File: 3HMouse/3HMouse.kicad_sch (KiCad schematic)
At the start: 85 parts, among them J1 USB_C_Receptacle_USB2.0, SW1 CherryMX, SW10 CherryMX, SW11 CherryMX, SW12 CherryMX, SW13 CherryMX, SW14 CherryMX, SW15 CherryMX, SW16 CherryMX, SW17 CherryMX, SW18 CherryMX, SW19 CherryMX, SW2 CherryMX, SW20 CherryMX, SW21 CherryMX, SW22 CherryMX, SW23 CherryMX, SW24 CherryMX, SW25 CherryMX, SW26 CherryMX, SW27 CherryMX, SW28 CherryMX, SW29 CherryMX, SW3 CherryMX, SW30 RotaryEncoder, SW31 RotaryEncoder, SW32 Reset, SW4 CherryMX, SW5 CherryMX, SW6 CherryMX, SW7 CherryMX, SW8 CherryMX, SW9 CherryMX, U1 AT90USB1286-A, U2 USBLC6-2SC6, Y1 16 MHz

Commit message: v0.4.0 final
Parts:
- removed SW32: Reset, random-keyboard-parts:SKQG-1155865, symbol Switch:SW_Push
- removed U1: AT90USB1286-A, Package_QFP:TQFP-64_14x14mm_P0.8mm, symbol MCU_Microchip_AVR:AT90USB1286-A
- added S2: TS-1187A-B-A-B, SW_TS-1187A-B-A-B:SW_TS-1187A-B-A-B, symbol TS-1187A-B-A-B:TS-1187A-B-A-B
- added U1: ATmega32U4-M, Package_DFN_QFN:QFN-44-1EP_7x7mm_P0.5mm_EP5.2x5.2mm, symbol MCU_Microchip_ATmega:ATmega32U4-M
- J1: footprint Connector_USB:USB_C_Receptacle_GCT_USB4085 -> USB_C_Receptacle_GT-USB-7010:USB_C_Receptacle_GT-USB-7010
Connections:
- net +5V: now also C3.1, U1.14 (VCC), U1.2 (UVCC), U1.24 (AVCC), U1.34 (VCC), U1.44 (AVCC), U1.7 (VBUS); no longer C3.2
- net COL0: now also U1.11 (PB3)
- net COL1: now also U1.19 (PD1)
- net COL10: now also U1.1 (PE6)
- net COL2: now also U1.20 (PD2)
- net COL3: now also U1.21 (PD3)
- net COL4: now also U1.22 (PD5)
- net COL5: now also U1.36 (PF7)
- net COL6: now also U1.25 (PD4)
- net COL7: now also U1.26 (PD6)
- net COL8: now also U1.27 (PD7)
- net COL9: now also U1.28 (PB4)
- net GND: now also C3.2, C4.1, C5.1, C6.1, R5.2, S2.A, S2.B, U1.15 (GND), U1.23 (GND), U1.35 (GND), U1.43 (GND), U1.45 (GND), U1.5 (UGND); no longer R5.1
- net HOR: now also U1.40 (PF1)
- net RE0A: now also U1.30 (PB6)
- net RE0B: now also U1.29 (PB5)
- net RE1A: now also U1.32 (PC7)
- net RE1B: now also U1.31 (PC6)
- net ROW0: now also U1.9 (PB1)
- net ROW1: now also U1.10 (PB2)
- net ROW2: now also U1.12 (PB7)
- net ROW3: now also U1.8 (PB0)
- net ROW4: now also U1.39 (PF4)
- net SCL: now also U1.37 (PF6)
- net SDA: now also U1.38 (PF5)
- net VER: now also U1.41 (PF0)
- net XTAL1: now reaches C1.1, Y1.1
- net XTAL1: now also U1.17 (XTAL1)
- net D-F: now reaches R2.2
- net D-F: now also U1.3 (D-)
- net XTAL2: now reaches C2.1, Y1.3
- net XTAL2: now also U1.16 (XTAL2)
- net RESET: now reaches R6.2
- net RESET: now also S2.C, S2.D, U1.13 (~{RESET})
- net D+F: now reaches R1.2
- net D+F: now also U1.4 (D+)
- net UCAP: now reaches C8.2
- net UCAP: now also U1.6 (UCAP)
- new net: R5.1, U1.33 (~{HWB}/PE2)
- no-connect marks 34 -> 12
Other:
- moved on the sheet: C3, C4, C5, C6, C7, C8, R5, R6

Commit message: Placements done for v2
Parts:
- removed D20, D21, D22, D23, D24, D25, D26, D27, D28, D29, D35: D_Small, Diode_SMD:D_SOD-123, symbol Device:D_Small
- removed SW20, SW21, SW22, SW23, SW24, SW25, SW26, SW27, SW28, SW29: CherryMX, MX_Only:MXOnly-1U-NoLED, symbol CherryMX:CherryMX
- removed SW30, SW31: RotaryEncoder, Keebio-Parts:RotaryEncoder_EC11, symbol Device:RotaryEncoder
- added D0_3, D1_3, D2_3, D5_0, D5_1, D5_2, D5_3, D5_4, D6_0, D6_1, D6_2, D6_3, D6_4: D_Small, Diode_SMD:D_SOD-123, symbol Device:D_Small
- added DL0_0, DL0_1, DL0_2, DL1_0, DL1_1, DL1_2, DL2_0, DL2_1, DL2_2, DL3_0, DL3_1, DL3_2, DL3_3, DL3_4, DL4_0, DL4_1, DL4_2, DL4_3, DL4_4, DL5_0, DL5_1, DL5_2, DL5_3, DL5_4, DL6_0, DL6_1, DL6_2, DL6_3, DL6_4: SK6805-EC15, HLibrary:SK6805-EC15, symbol HLibrary:SK6805-EC15
- added R8: 500, Resistor_SMD:R_0805_2012Metric, symbol Device:R_Small
- added RE1, RE2: RotaryEncoder_Switch, Rotary_Encoder:RotaryEncoder_Alps_EC11E-Switch_Vertical_H20mm, symbol Device:RotaryEncoder_Switch
- added SW5_0, SW5_1, SW5_2, SW5_3, SW5_4, SW6_0, SW6_1, SW6_2, SW6_3, SW6_4: CherryMX, MX_Only:MXOnly-1U-Hotswap, symbol CherryMX:CherryMX
- SW0_0: renamed from SW1; footprint MX_Only:MXOnly-1U-NoLED -> MX_Only:MXOnly-1U-Hotswap
- SW0_1: renamed from SW6; footprint MX_Only:MXOnly-1U-NoLED -> MX_Only:MXOnly-1U-Hotswap
- SW0_2: renamed from SW11; footprint MX_Only:MXOnly-1U-NoLED -> MX_Only:MXOnly-1U-Hotswap
- SW1_0: renamed from SW2; footprint MX_Only:MXOnly-1U-NoLED -> MX_Only:MXOnly-1U-Hotswap
- SW1_1: renamed from SW7; footprint MX_Only:MXOnly-1U-NoLED -> MX_Only:MXOnly-1U-Hotswap
- SW1_2: renamed from SW12; footprint MX_Only:MXOnly-1U-NoLED -> MX_Only:MXOnly-1U-Hotswap
- SW2_0: renamed from SW3; footprint MX_Only:MXOnly-1U-NoLED -> MX_Only:MXOnly-1U-Hotswap
- SW2_1: renamed from SW8; footprint MX_Only:MXOnly-1U-NoLED -> MX_Only:MXOnly-1U-Hotswap
- SW2_2: renamed from SW13; footprint MX_Only:MXOnly-1U-NoLED -> MX_Only:MXOnly-1U-Hotswap
- SW3_0: renamed from SW4; footprint MX_Only:MXOnly-1.5U-NoLED -> MX_Only:MXOnly-1U-Hotswap
- SW3_1: renamed from SW9; footprint MX_Only:MXOnly-1U-NoLED -> MX_Only:MXOnly-1U-Hotswap
- SW3_2: renamed from SW14; footprint MX_Only:MXOnly-1U-NoLED -> MX_Only:MXOnly-1U-Hotswap
- SW3_3: renamed from SW16; footprint MX_Only:MXOnly-1U-NoLED -> MX_Only:MXOnly-1U-Hotswap
- SW3_4: renamed from SW18; footprint MX_Only:MXOnly-1U-NoLED -> MX_Only:MXOnly-1U-Hotswap
- SW4_0: renamed from SW5; footprint MX_Only:MXOnly-1.25U-NoLED -> MX_Only:MXOnly-1U-Hotswap
- SW4_1: renamed from SW10; footprint MX_Only:MXOnly-1.25U-NoLED -> MX_Only:MXOnly-1U-Hotswap
- SW4_2: renamed from SW15; footprint MX_Only:MXOnly-1U-NoLED -> MX_Only:MXOnly-1U-Hotswap
- SW4_3: renamed from SW17; footprint MX_Only:MXOnly-1U-NoLED -> MX_Only:MXOnly-1U-Hotswap
- SW4_4: renamed from SW19; footprint MX_Only:MXOnly-1U-NoLED -> MX_Only:MXOnly-1U-Hotswap
- renumbered D1 to D0_0, D6 to D0_1, D11 to D0_2, D2 to D1_0, D7 to D1_1, D12 to D1_2, D3 to D2_0, D8 to D2_1, D13 to D2_2, D4 to D3_0, D9 to D3_1, D14 to D3_2, D16 to D3_3, D18 to D3_4, D5 to D4_0, D10 to D4_1, D15 to D4_2, D17 to D4_3, D19 to D4_4
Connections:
- net +5V: now also DL0_0.2 (VDD), DL0_1.2 (VDD), DL0_2.2 (VDD), DL1_0.2 (VDD), DL1_1.2 (VDD), DL1_2.2 (VDD), DL2_0.2 (VDD), DL2_1.2 (VDD), DL2_2.2 (VDD), DL3_0.2 (VDD), DL3_1.2 (VDD), DL3_2.2 (VDD), DL3_3.2 (VDD), DL3_4.2 (VDD), DL4_0.2 (VDD), DL4_1.2 (VDD), DL4_2.2 (VDD), DL4_3.2 (VDD), DL4_4.2 (VDD), DL5_0.2 (VDD), DL5_1.2 (VDD), DL5_2.2 (VDD), DL5_3.2 (VDD), DL5_4.2 (VDD), DL6_0.2 (VDD), DL6_1.2 (VDD), DL6_2.2 (VDD), DL6_3.2 (VDD), DL6_4.2 (VDD)
- net COL0: now also SW5_0.2, SW6_0.2
- net COL1: now also SW5_1.2, SW6_1.2
- net COL2: now also SW5_2.2, SW6_2.2
- net COL3: now also S1.C1, RE1.S1, RE2.S1, SW5_3.2, SW6_3.2
- net COL4: now also SW5_4.2, SW6_4.2
- net GND: now also DL0_0.4 (GND), DL0_1.4 (GND), DL0_2.4 (GND), DL1_0.4 (GND), DL1_1.4 (GND), DL1_2.4 (GND), DL2_0.4 (GND), DL2_1.4 (GND), DL2_2.4 (GND), DL3_0.4 (GND), DL3_1.4 (GND), DL3_2.4 (GND), DL3_3.4 (GND), DL3_4.4 (GND), DL4_0.4 (GND), DL4_1.4 (GND), DL4_2.4 (GND), DL4_3.4 (GND), DL4_4.4 (GND), DL5_0.4 (GND), DL5_1.4 (GND), DL5_2.4 (GND), DL5_3.4 (GND), DL5_4.4 (GND), DL6_0.4 (GND), DL6_1.4 (GND), DL6_2.4 (GND), DL6_3.4 (GND), DL6_4.4 (GND), RE1.C, RE2.C
- net RE0A: now also RE1.A
- net RE0B: now also RE1.B
- net RE1A: now also RE2.A
- net RE1B: now also RE2.B
- net ROW0: now also D0_3.1 (K)
- net ROW1: now also D1_3.1 (K)
- net ROW2: now also D2_3.1 (K)
- net LED: now reaches U1.18 (PD0)
- net LED: now also R8.1
- net at S1.D1: now also D0_3.2 (A)
- net COL10: no longer names the net of U1.1 (PE6)
- net COL10: no longer S1.C1
- net COL5: no longer names the net of U1.36 (PF7)
- net COL6 renamed ROW6
- net ROW6: now also D6_0.1 (K), D6_1.1 (K), D6_2.1 (K), D6_3.1 (K), D6_4.1 (K)
- net COL7: no longer names the net of U1.26 (PD6)
- net COL8: no longer names the net of U1.27 (PD7)
- net COL9 renamed ROW5
- net ROW5: now also D5_0.1 (K), D5_1.1 (K), D5_2.1 (K), D5_3.1 (K), D5_4.1 (K)
- new net: D6_2.2 (A), SW6_2.1
- new net: DL2_1.3 (DOUT), DL2_2.1 (DIN)
- new net: DL2_2.3 (DOUT), DL3_0.1 (DIN)
- new net: D6_3.2 (A), SW6_3.1
- new net: DL3_3.3 (DOUT), DL3_4.1 (DIN)
- new net: DL3_4.3 (DOUT), DL4_0.1 (DIN)
- new net: DL1_0.3 (DOUT), DL1_1.1 (DIN)
- new net: DL1_1.3 (DOUT), DL1_2.1 (DIN)
- new net: D5_0.2 (A), SW5_0.1
- new net: D6_4.2 (A), SW6_4.1
- new net: DL4_4.3 (DOUT), DL5_0.1 (DIN)
- new net: DL5_0.3 (DOUT), DL5_1.1 (DIN)
- new net: DL0_2.3 (DOUT), DL1_0.1 (DIN)
- new net: D6_1.2 (A), SW6_1.1
- new net: D2_3.2 (A), RE2.S2
- new net: DL4_0.3 (DOUT), DL4_1.1 (DIN)
- new net: DL4_1.3 (DOUT), DL4_2.1 (DIN)
- new net: DL0_0.1 (DIN), R8.2
- new net: DL0_0.3 (DOUT), DL0_1.1 (DIN)
- new net: DL5_2.3 (DOUT), DL5_3.1 (DIN)
- new net: DL5_3.3 (DOUT), DL5_4.1 (DIN)
- new net: DL3_0.3 (DOUT), DL3_1.1 (DIN)
- new net: DL4_2.3 (DOUT), DL4_3.1 (DIN)
- new net: DL4_3.3 (DOUT), DL4_4.1 (DIN)
- new net: D1_3.2 (A), RE1.S2
- new net: DL1_2.3 (DOUT), DL2_0.1 (DIN)
- new net: DL2_0.3 (DOUT), DL2_1.1 (DIN)
- new net: D6_0.2 (A), SW6_0.1
- new net: DL6_2.3 (DOUT), DL6_3.1 (DIN)
- new net: DL6_3.3 (DOUT), DL6_4.1 (DIN)
- new net: DL3_1.3 (DOUT), DL3_2.1 (DIN)
- new net: D5_2.2 (A), SW5_2.1
- new net: D5_3.2 (A), SW5_3.1
- new net: D5_1.2 (A), SW5_1.1
- new net: DL0_1.3 (DOUT), DL0_2.1 (DIN)
- new net: D5_4.2 (A), SW5_4.1
- new net: DL5_4.3 (DOUT), DL6_0.1 (DIN)
- new net: DL3_2.3 (DOUT), DL3_3.1 (DIN)
- new net: DL6_0.3 (DOUT), DL6_1.1 (DIN)
- new net: DL6_1.3 (DOUT), DL6_2.1 (DIN)
- new net: DL5_1.3 (DOUT), DL5_2.1 (DIN)
- no-connect marks 12 -> 16
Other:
- note added: "RGB LEDs"
- note removed: "3HMouse"
- moved on the sheet: Brd1, C1, C2, C3, C4, C5, C6, C7, C8, D0_0, D0_1, D0_2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

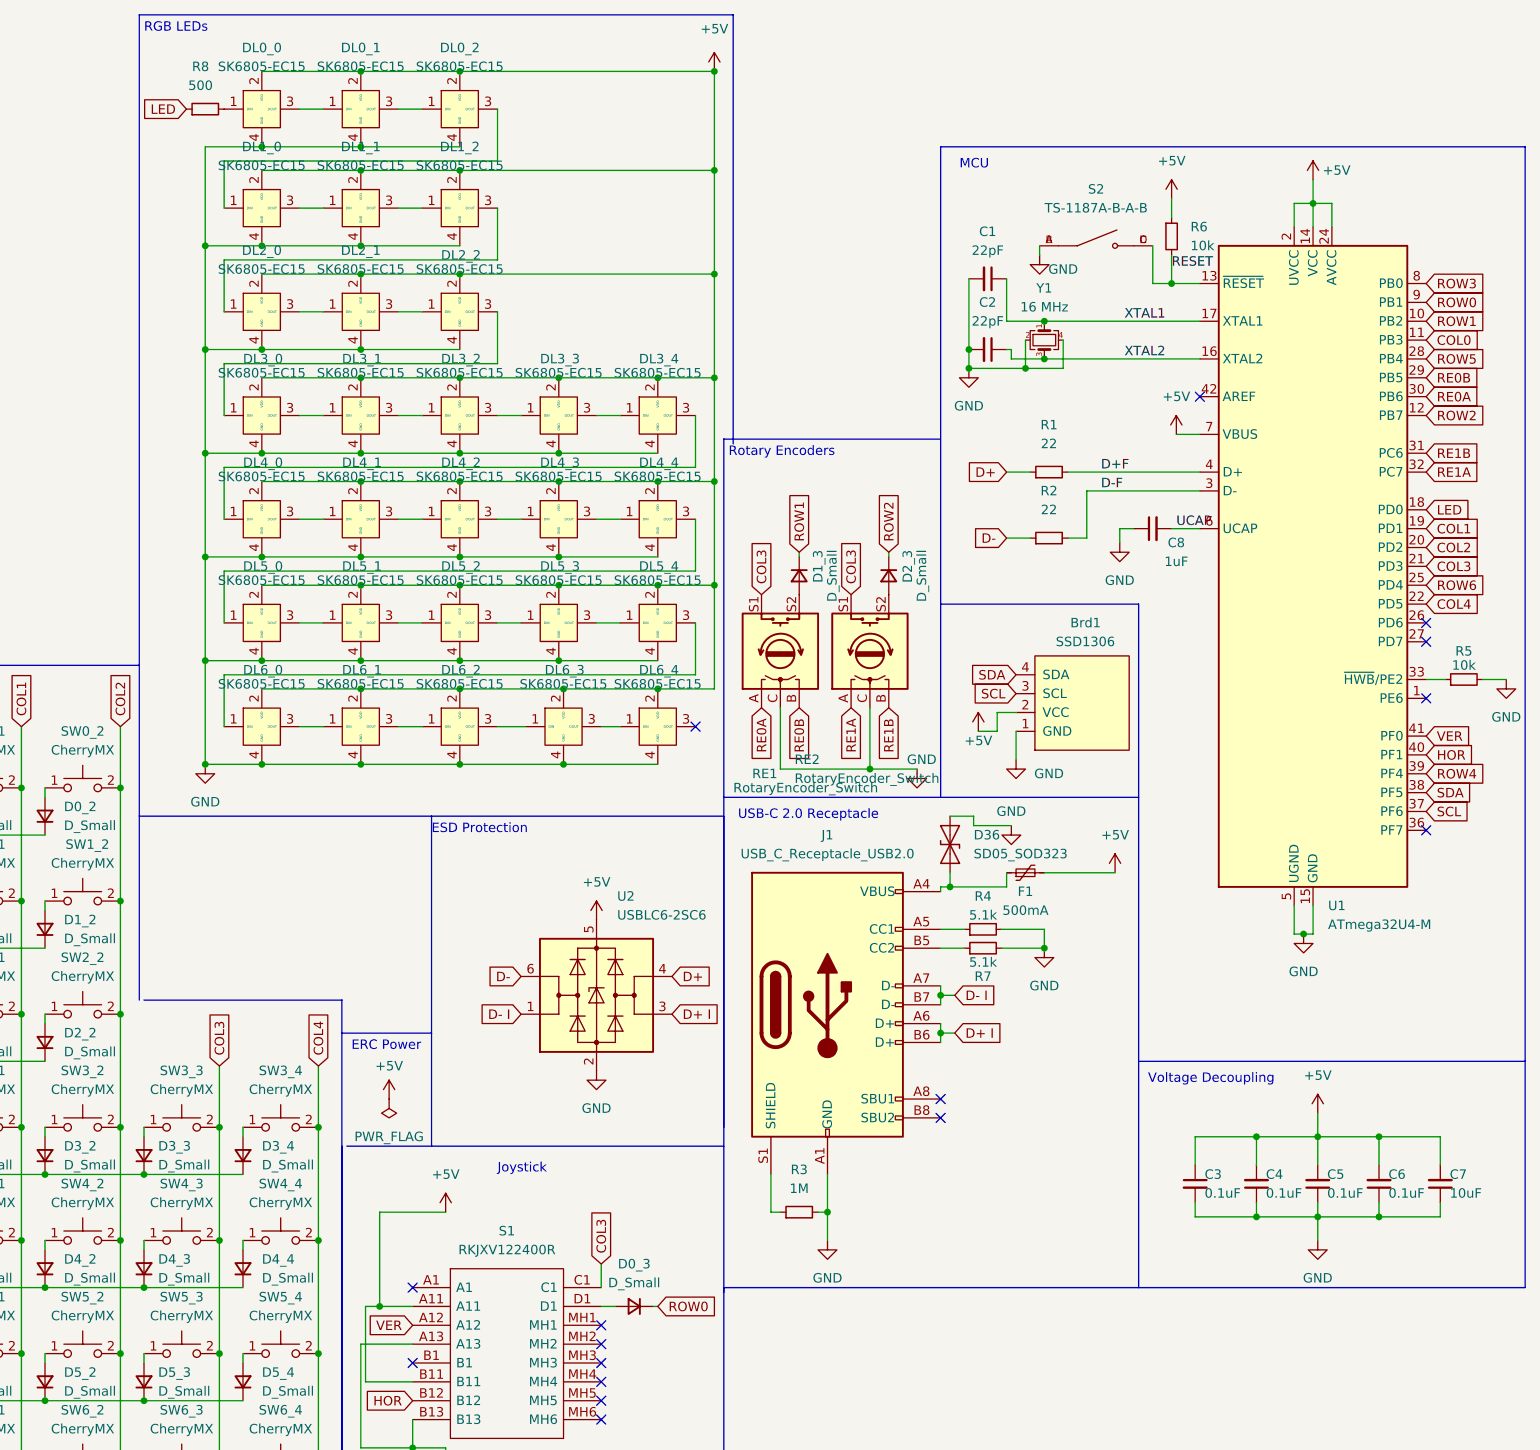
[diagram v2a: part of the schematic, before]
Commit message: LED and switch routing
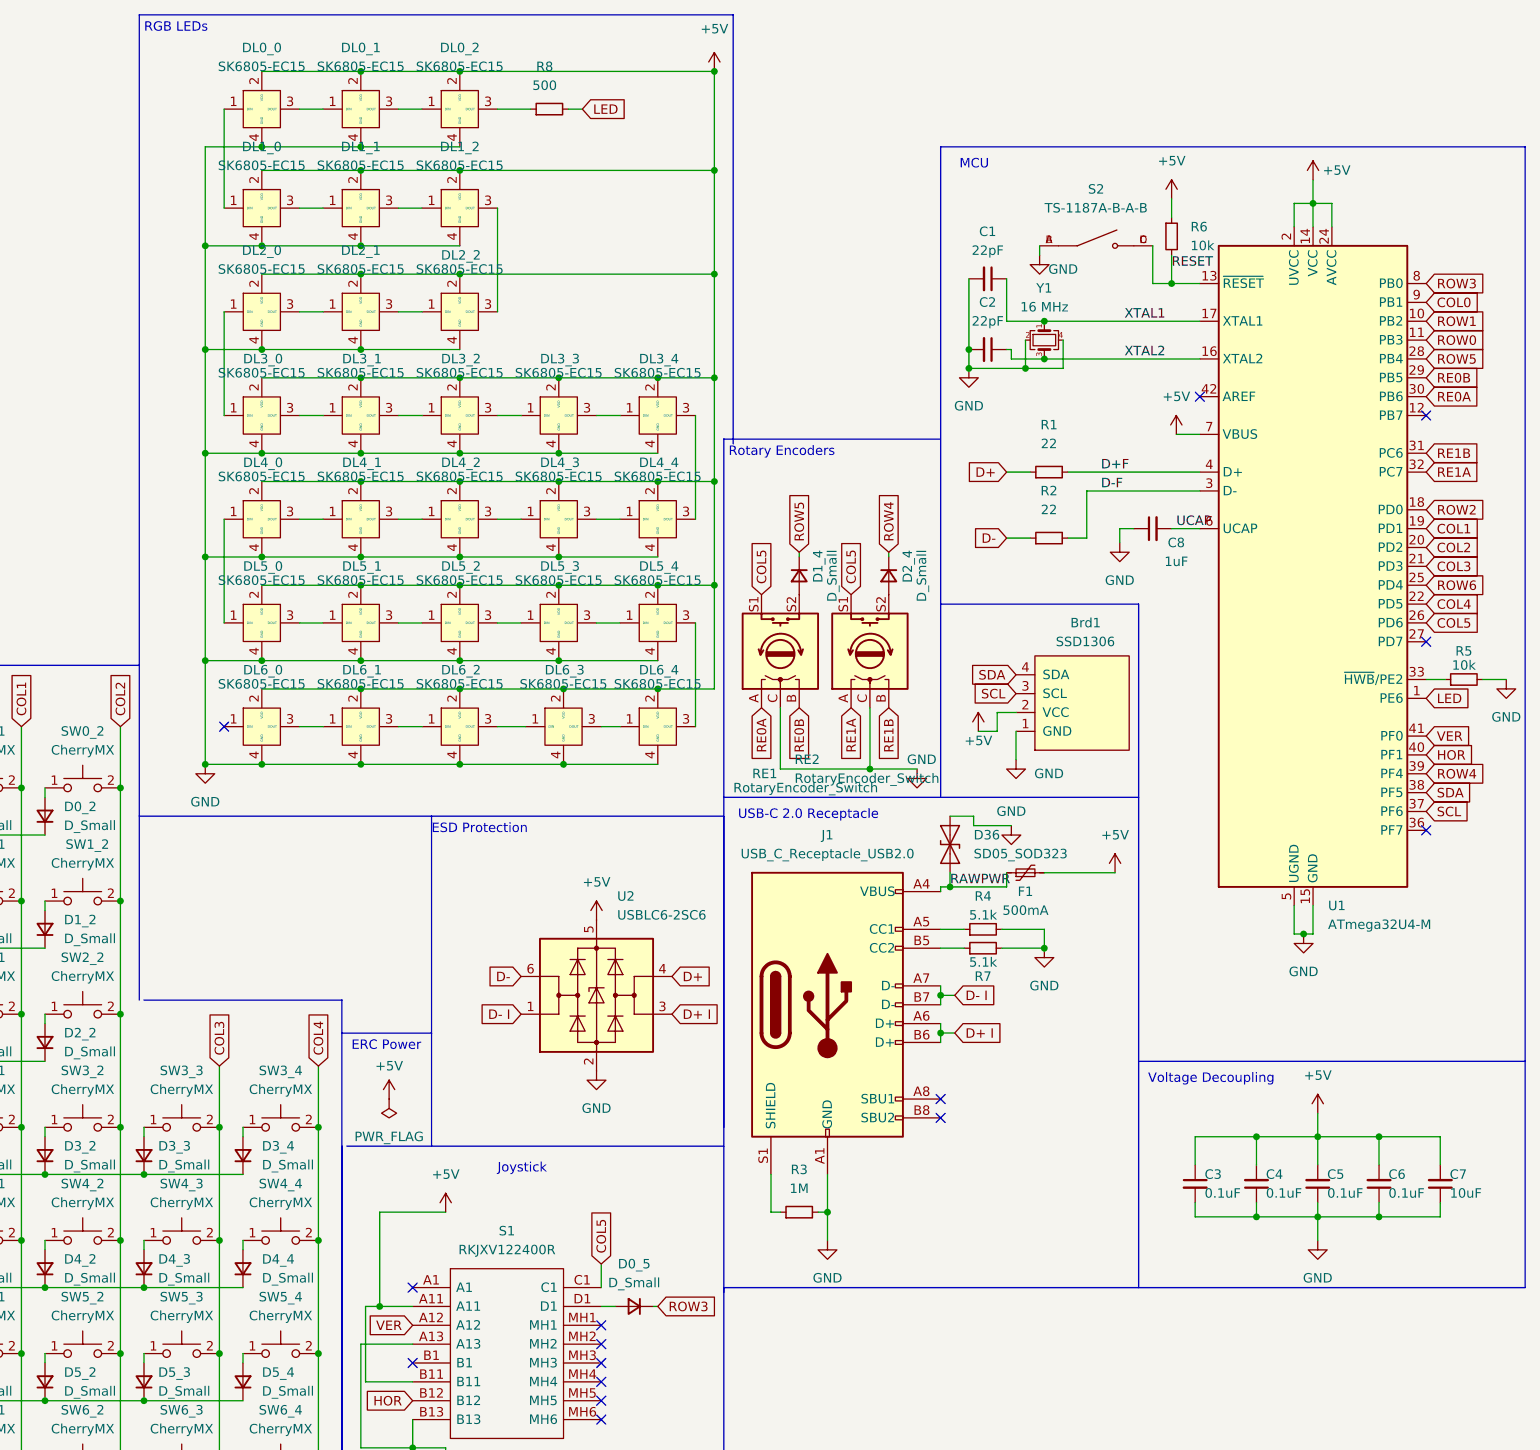
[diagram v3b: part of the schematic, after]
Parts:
- renumbered D0_3 to D0_5, D1_3 to D1_4, D2_3 to D2_4
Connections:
- net COL0: now also U1.9 (PB1); no longer U1.11 (PB3)
- net COL3: no longer RE1.S1, RE2.S1, S1.C1
- net LED: now also R8.2, U1.1 (PE6); no longer R8.1, U1.18 (PD0)
- net ROW0: now also U1.11 (PB3); no longer D0_5.1 (K), U1.9 (PB1)
- net ROW1: no longer D1_4.1 (K)
- net ROW2: now also U1.18 (PD0); no longer D2_4.1 (K), U1.12 (PB7)
- net ROW3: now also D0_5.1 (K)
- net ROW4: now also D2_4.1 (K)
- net ROW5: now also D1_4.1 (K)
- net at DL2_2.3 (DOUT): now also DL1_2.3 (DOUT); no longer DL3_0.1 (DIN)
- net at DL3_4.3 (DOUT): now also DL4_4.3 (DOUT); no longer DL4_0.1 (DIN)
- net COL5: now reaches U1.26 (PD6)
- net COL5: now also RE1.S1, RE2.S1, S1.C1
- net at DL5_0.1 (DIN): now also DL4_0.1 (DIN); no longer DL4_4.3 (DOUT)
- net at DL1_0.1 (DIN): now also DL0_0.1 (DIN); no longer DL0_2.3 (DOUT)
- net at DL2_0.1 (DIN): now also DL3_0.1 (DIN); no longer DL1_2.3 (DOUT)
- net RAWPWR: now reaches D36.1 (A1), F1.1, J1.A4 (VBUS), J1.A9 (VBUS), J1.B4 (VBUS), J1.B9 (VBUS)
- net at DL5_4.3 (DOUT): now also DL6_4.3 (DOUT); no longer DL6_0.1 (DIN)
- new net: DL0_2.3 (DOUT), R8.1
- no-connect marks 16 -> 15
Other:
- moved on the sheet: R8

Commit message: v2 Done
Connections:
- net COL0: now also U1.18 (PD0); no longer U1.9 (PB1)
- net COL1: now also U1.20 (PD2); no longer U1.19 (PD1)
- net COL2: now also U1.22 (PD5); no longer U1.20 (PD2)
- net COL3: now also U1.25 (PD4); no longer U1.21 (PD3)
- net COL4: now also U1.40 (PF1); no longer U1.22 (PD5)
- net COL5: now also U1.37 (PF6); no longer U1.26 (PD6)
- net HOR: now also U1.39 (PF4); no longer U1.40 (PF1)
- net LED: now also U1.12 (PB7); no longer U1.1 (PE6)
- net RE1A: now also RE1.A, U1.31 (PC6); no longer RE2.A, U1.32 (PC7)
- net RE1B: now also RE1.B, U1.30 (PB6); no longer RE2.B, U1.31 (PC6)
- net ROW0: now also U1.19 (PD1); no longer U1.11 (PB3)
- net ROW1: now also U1.21 (PD3); no longer U1.10 (PB2)
- net ROW2: now also U1.11 (PB3); no longer U1.18 (PD0)
- net ROW3: now also U1.26 (PD6); no longer U1.8 (PB0)
- net ROW4: now also U1.27 (PD7); no longer U1.39 (PF4)
- net ROW6: now also U1.29 (PB5); no longer U1.25 (PD4)
- net SCL: now also U1.9 (PB1); no longer U1.37 (PF6)
- net SDA: now also U1.8 (PB0); no longer U1.38 (PF5)
- net VER: now also U1.38 (PF5); no longer U1.41 (PF0)
- net RE2B: now reaches U1.36 (PF7)
- net RE2B: now also RE2.B
- removed net RE0A: RE1.A, U1.30 (PB6)
- removed net RE0B: RE1.B, U1.29 (PB5)
- new net RE2A: RE2.A, U1.32 (PC7)

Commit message: v2.1.0
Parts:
- added H1, H2, H3, H4, H5: MountingHole, MountingHole:MountingHole_2.2mm_M2_Pad, symbol Mechanical:MountingHole_Pad
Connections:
- net COL0: now also U1.27 (PD7); no longer U1.18 (PD0)
- net COL1: now also U1.28 (PB4); no longer U1.20 (PD2)
- net COL2: now also U1.29 (PB5); no longer U1.22 (PD5)
- net COL3: now also U1.32 (PC7); no longer U1.25 (PD4)
- net COL4: now also U1.37 (PF6); no longer U1.40 (PF1)
- net COL5: now also U1.12 (PB7); no longer U1.37 (PF6)
- net GND: now also H2.1
- net HOR: now also U1.41 (PF0); no longer U1.39 (PF4)
- net LED: now also U1.25 (PD4); no longer U1.12 (PB7)
- net RE1A: now also U1.9 (PB1); no longer U1.31 (PC6)
- net RE1B: now also U1.8 (PB0); no longer U1.30 (PB6)
- net RE2A: now also U1.11 (PB3); no longer U1.32 (PC7)
- net RE2B: now also U1.10 (PB2); no longer U1.36 (PF7)
- net ROW0: now also U1.26 (PD6); no longer U1.19 (PD1)
- net ROW1: now also U1.30 (PB6); no longer U1.21 (PD3)
- net ROW2: now also U1.31 (PC6); no longer U1.11 (PB3)
- net ROW3: now also U1.36 (PF7); no longer U1.26 (PD6)
- net ROW4: now also U1.38 (PF5); no longer U1.27 (PD7)
- net ROW5: now also U1.39 (PF4); no longer U1.28 (PB4)
- net ROW6: now also U1.1 (PE6); no longer U1.29 (PB5)
- net SCL: now also U1.18 (PD0); no longer U1.9 (PB1)
- net SDA: now also U1.19 (PD1); no longer U1.8 (PB0)
- net VER: now also U1.40 (PF1); no longer U1.38 (PF5)
- net D+ I renamed DI+
- net D+F renamed DF+
- net D- I renamed DI-
- net D-F renamed DF-
- no-connect marks 15 -> 19
